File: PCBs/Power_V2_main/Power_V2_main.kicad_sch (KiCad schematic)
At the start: 3 parts

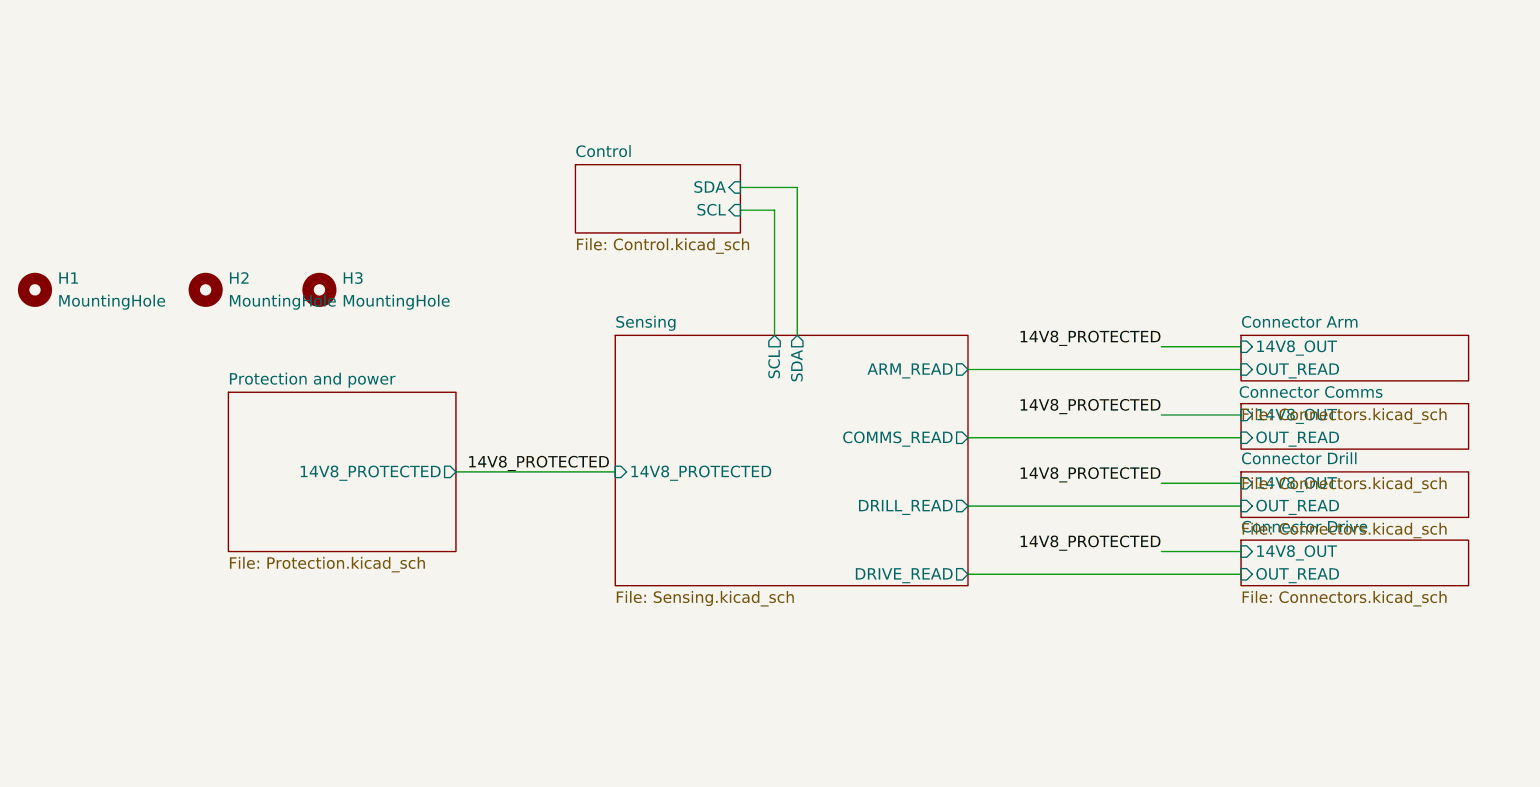
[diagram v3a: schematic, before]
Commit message: added LED indicators to board and redid power distribution in PCIe
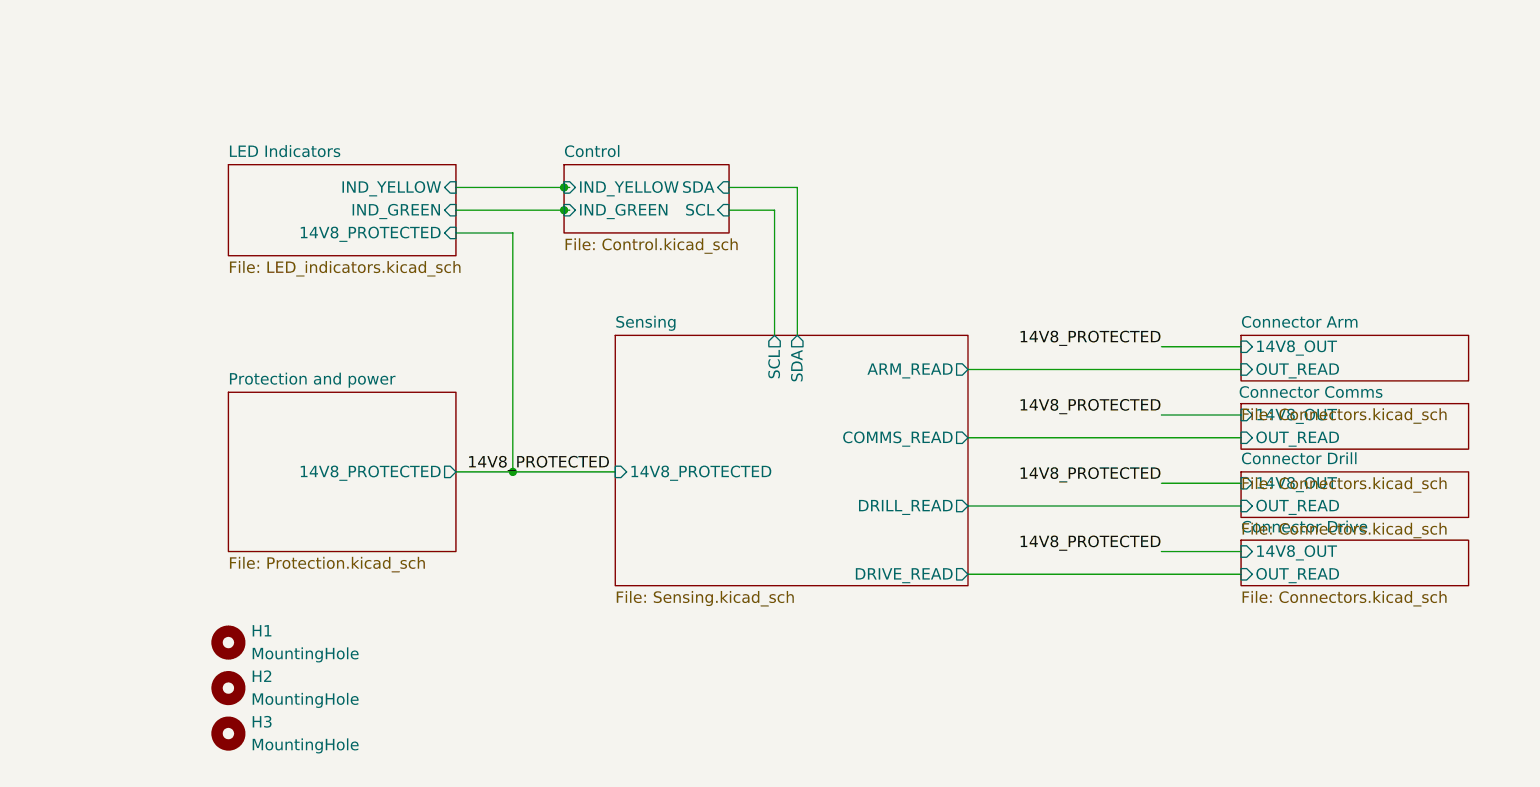
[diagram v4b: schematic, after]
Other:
- added sheet LED Indicators (LED_indicators.kicad_sch)
- sheet Control ports: added IND_GREEN, IND_YELLOW; removed none
- moved on the sheet: H1, H2, H3
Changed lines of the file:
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@@
 	(generator_version "9.0")
 	(paper "A4")
+	(junction
+		(at 120.015 66.04)
+		(diameter 0)
+		(color 0 0 0 0)
+	)
+	(junction
+		(at 120.015 63.5)
+		(diameter 0)
+		(color 0 0 0 0)
+	)
+	(junction
+		(at 114.3 95.25)
+		(diameter 0)
+		(color 0 0 0 0)
+	)
 	(wire
 		(pts
@@
 	(wire
 		(pts
+			(xy 114.3 95.25) (xy 125.73 95.25)
+		)
+		(stroke
+			(width 0)
+			(type default)
+		)
+	)
+	(wire
+		(pts
 			(xy 165.1 91.44) (xy 195.58 91.44)
 		)
@@
 	(wire
 		(pts
+			(xy 120.015 63.5) (xy 120.65 63.5)
+		)
+		(stroke
+			(width 0)
+			(type default)
+		)
+	)
+	(wire
+		(pts
+			(xy 107.95 66.04) (xy 120.015 66.04)
+		)
+		(stroke
+			(width 0)
+			(type default)
+		)
+	)
+	(wire
+		(pts
+			(xy 114.3 68.58) (xy 114.3 95.25)
+		)
+		(stroke
+			(width 0)
+			(type default)
+		)
+	)
+	(wire
+		(pts
 			(xy 165.1 106.68) (xy 195.58 106.68)
 		)
@@
 	(wire
 		(pts
+			(xy 120.015 66.04) (xy 120.65 66.04)
+		)
+		(stroke
+			(width 0)
+			(type default)
+		)
+	)
+	(wire
+		(pts
 			(xy 165.1 83.82) (xy 195.58 83.82)
 		)
@@
 	(wire
 		(pts
-			(xy 139.7 66.04) (xy 143.51 66.04)
+			(xy 107.95 63.5) (xy 120.015 63.5)
+		)
+		(stroke
+			(width 0)
+			(type default)
+		)
+	)
+	(wire
+		(pts
+			(xy 107.95 68.58) (xy 114.3 68.58)
+		)
+		(stroke
+			(width 0)
+			(type default)
+		)
+	)
+	(wire
+		(pts
+			(xy 138.43 66.04) (xy 143.51 66.04)
 		)
 		(stroke
@@
 	(wire
 		(pts
-			(xy 107.95 95.25) (xy 125.73 95.25)
+			(xy 107.95 95.25) (xy 114.3 95.25)
 		)
 		(stroke
@@
 	(wire
 		(pts
-			(xy 139.7 63.5) (xy 146.05 63.5)
+			(xy 138.43 63.5) (xy 146.05 63.5)
 		)
 		(stroke
@@
 	(symbol
 		(lib_id "Mechanical:MountingHole")
-		(at 92.71 74.93 0)
+		(at 82.55 124.46 0)
 		(unit 1)
 		(exclude_from_sim no)
@@
 		(fields_autoplaced yes)
 		(property "Reference" "H3"
-			(at 95.25 73.6599 0)
+			(at 85.09 123.1899 0)
 			(effects
 				(font
@@
 		)
 		(property "Value" "MountingHole"
-			(at 95.25 76.1999 0)
+			(at 85.09 125.7299 0)
 			(effects
 				(font
@@
 		)
 		(property "Footprint" "MountingHole:MountingHole_2.5mm"
-			(at 92.71 74.93 0)
+			(at 82.55 124.46 0)
 			(effects
 				(font
@@
 		)
 		(property "Datasheet" "~"
-			(at 92.71 74.93 0)
+			(at 82.55 124.46 0)
 			(effects
 				(font
@@
 		)
 		(property "Description" "Mounting Hole without connection"
-			(at 92.71 74.93 0)
+			(at 82.55 124.46 0)
 			(effects
 				(font
@@
 	(symbol
 		(lib_id "Mechanical:MountingHole")
-		(at 80.01 74.93 0)
+		(at 82.55 119.38 0)
 		(unit 1)
 		(exclude_from_sim no)
@@
 		(fields_autoplaced yes)
 		(property "Reference" "H2"
-			(at 82.55 73.6599 0)
+			(at 85.09 118.1099 0)
 			(effects
 				(font
@@
 		)
 		(property "Value" "MountingHole"
-			(at 82.55 76.1999 0)
+			(at 85.09 120.6499 0)
 			(effects
 				(font
@@
 		)
 		(property "Footprint" "MountingHole:MountingHole_2.5mm"
-			(at 80.01 74.93 0)
+			(at 82.55 119.38 0)
 			(effects
 				(font
@@
 		)
 		(property "Datasheet" "~"
-			(at 80.01 74.93 0)
+			(at 82.55 119.38 0)
 			(effects
 				(font
@@
 		)
 		(property "Description" "Mounting Hole without connection"
-			(at 80.01 74.93 0)
+			(at 82.55 119.38 0)
 			(effects
 				(font
@@
 	(symbol
 		(lib_id "Mechanical:MountingHole")
-		(at 60.96 74.93 0)
+		(at 82.55 114.3 0)
 		(unit 1)
 		(exclude_from_sim no)
@@
 		(fields_autoplaced yes)
 		(property "Reference" "H1"
-			(at 63.5 73.6599 0)
+			(at 85.09 113.0299 0)
 			(effects
 				(font
@@
 		)
 		(property "Value" "MountingHole"
-			(at 63.5 76.1999 0)
+			(at 85.09 115.5699 0)
 			(effects
 				(font
@@
 		)
 		(property "Footprint" "MountingHole:MountingHole_2.5mm"
-			(at 60.96 74.93 0)
+			(at 82.55 114.3 0)
 			(effects
 				(font
@@
 		)
 		(property "Datasheet" "~"
-			(at 60.96 74.93 0)
+			(at 82.55 114.3 0)
 			(effects
 				(font
@@
 		)
 		(property "Description" "Mounting Hole without connection"
-			(at 60.96 74.93 0)
+			(at 82.55 114.3 0)
 			(effects
 				(font
@@
 	)
 	(sheet
-		(at 121.285 60.96)
+		(at 120.015 60.96)
 		(size 18.415 7.62)
 		(exclude_from_sim no)
@@
 		)
 		(property "Sheetname" "Control"
-			(at 121.285 60.2484 0)
+			(at 120.015 60.2484 0)
 			(effects
 				(font
@@
 		)
 		(property "Sheetfile" "Control.kicad_sch"
-			(at 121.285 69.1646 0)
+			(at 120.015 69.1646 0)
 			(effects
 				(font
@@
 		)
 		(pin "SCL" input
-			(at 139.7 66.04 0)
+			(at 138.43 66.04 0)
 			(effects
 				(font
@@
 		)
 		(pin "SDA" input
-			(at 139.7 63.5 0)
-			(effects
-				(font
-					(size 1.27 1.27)
-				)
-				(justify right)
+			(at 138.43 63.5 0)
+			(effects
+				(font
+					(size 1.27 1.27)
+				)
+				(justify right)
+			)
+		)
+		(pin "IND_GREEN" input
+			(at 120.015 66.04 180)
+			(effects
+				(font
+					(size 1.27 1.27)
+				)
+				(justify left)
+			)
+		)
+		(pin "IND_YELLOW" input
+			(at 120.015 63.5 180)
+			(effects
+				(font
+					(size 1.27 1.27)
+				)
+				(justify left)
 			)
 		)
@@
 				)
 			)
+		)
+	)
+	(sheet
+		(at 82.55 60.96)
+		(size 25.4 10.16)
+		(exclude_from_sim no)
+		(in_bom yes)
+		(on_board yes)
+		(dnp no)
+		(fields_autoplaced yes)
+		(stroke
+			(width 0.1524)
+			(type solid)
+		)
+		(fill
+			(color 0 0 0 0.0000)
+		)
+		(property "Sheetname" "LED Indicators"
+			(at 82.55 60.2484 0)
+			(effects
+				(font
+					(size 1.27 1.27)
+				)
+				(justify left bottom)
+			)
+		)
+		(property "Sheetfile" "LED_indicators.kicad_sch"
+			(at 82.55 71.7046 0)
+			(effects
+				(font
+					(size 1.27 1.27)
+				)
+				(justify left top)
+			)
+		)
+		(pin "14V8_PROTECTED" input
+			(at 107.95 68.58 0)
+			(effects
+				(font
+					(size 1.27 1.27)
+				)
+				(justify right)
+			)
+		)
+		(pin "IND_GREEN" input
+			(at 107.95 66.04 0)
+			(effects
+				(font
+					(size 1.27 1.27)
+				)
+				(justify right)
+			)
+		)
+		(pin "IND_YELLOW" input
+			(at 107.95 63.5 0)
+			(effects
+				(font
+					(size 1.27 1.27)
+				)
+				(justify right)
+			)
+		)
+		(instances
+			(project "Power_V2_main"
+				(path "/68375d53-ee5f-4f08-9b72-814cdcf8200e"
+					(page "9")
+				)
+			)

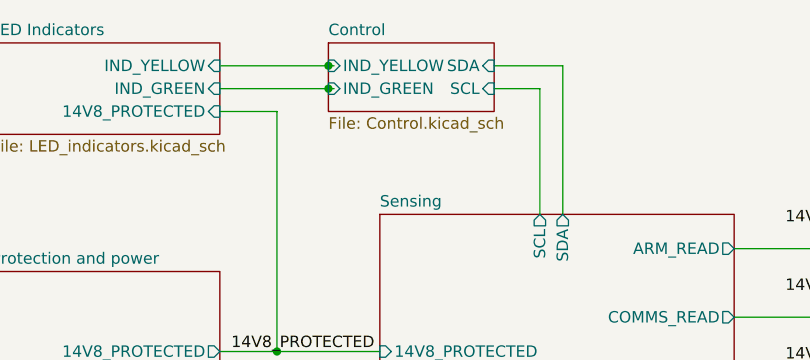
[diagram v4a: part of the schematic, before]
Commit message: modification to LED switches
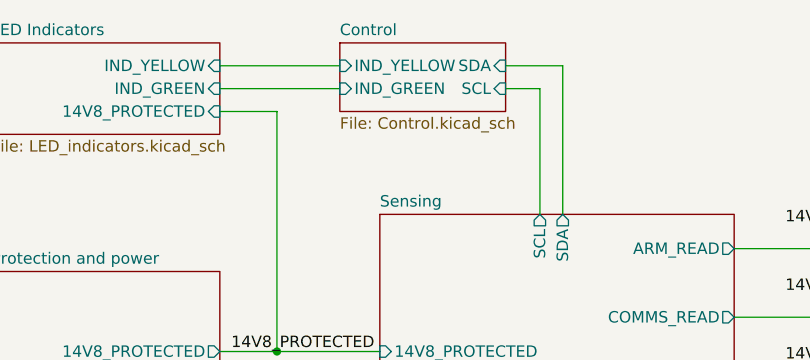
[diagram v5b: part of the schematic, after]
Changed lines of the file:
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@@
 	(paper "A4")
-	(junction
-		(at 120.015 66.04)
-		(diameter 0)
-		(color 0 0 0 0)
-	)
-	(junction
-		(at 120.015 63.5)
-		(diameter 0)
-		(color 0 0 0 0)
-	)
 	(junction
 		(at 114.3 95.25)
@@
 	(wire
 		(pts
-			(xy 120.015 63.5) (xy 120.65 63.5)
-		)
-		(stroke
-			(width 0)
-			(type default)
-		)
-	)
-	(wire
-		(pts
-			(xy 107.95 66.04) (xy 120.015 66.04)
+			(xy 107.95 66.04) (xy 121.285 66.04)
 		)
 		(stroke
@@
 	(wire
 		(pts
-			(xy 120.015 66.04) (xy 120.65 66.04)
-		)
-		(stroke
-			(width 0)
-			(type default)
-		)
-	)
-	(wire
-		(pts
 			(xy 165.1 83.82) (xy 195.58 83.82)
 		)
@@
 	(wire
 		(pts
-			(xy 107.95 63.5) (xy 120.015 63.5)
+			(xy 107.95 63.5) (xy 121.285 63.5)
 		)
 		(stroke
@@
 	(wire
 		(pts
-			(xy 138.43 66.04) (xy 143.51 66.04)
+			(xy 139.7 66.04) (xy 143.51 66.04)
 		)
 		(stroke
@@
 	(wire
 		(pts
-			(xy 138.43 63.5) (xy 146.05 63.5)
+			(xy 139.7 63.5) (xy 146.05 63.5)
 		)
 		(stroke
@@
 	)
 	(sheet
-		(at 120.015 60.96)
+		(at 121.285 60.96)
 		(size 18.415 7.62)
 		(exclude_from_sim no)
@@
 		)
 		(property "Sheetname" "Control"
-			(at 120.015 60.2484 0)
+			(at 121.285 60.2484 0)
 			(effects
 				(font
@@
 		)
 		(property "Sheetfile" "Control.kicad_sch"
-			(at 120.015 69.1646 0)
+			(at 121.285 69.1646 0)
 			(effects
 				(font
@@
 		)
 		(pin "SCL" input
-			(at 138.43 66.04 0)
+			(at 139.7 66.04 0)
 			(effects
 				(font
@@
 		)
 		(pin "SDA" input
-			(at 138.43 63.5 0)
+			(at 139.7 63.5 0)
 			(effects
 				(font
@@
 		)
 		(pin "IND_GREEN" input
-			(at 120.015 66.04 180)
+			(at 121.285 66.04 180)
 			(effects
 				(font
@@
 		)
 		(pin "IND_YELLOW" input
-			(at 120.015 63.5 180)
-			(effects
-				(font
+			(at 121.285 63.5 180)
+			(effects
+				(font

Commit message: follow up changes from meeting
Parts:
- H1, H2, H3: footprint MountingHole:MountingHole_2.5mm -> MountingHole:MountingHole_2.7mm_M2.5_DIN965_Pad_TopBottom
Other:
- sheet Control ports: added IND_SIREN; removed none
- sheet LED Indicators ports: added IND_SIREN; removed none
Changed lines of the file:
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@@
 	(wire
 		(pts
-			(xy 114.3 68.58) (xy 114.3 95.25)
+			(xy 114.3 71.12) (xy 114.3 95.25)
 		)
 		(stroke
@@
 	(wire
 		(pts
+			(xy 107.95 68.58) (xy 121.285 68.58)
+		)
+		(stroke
+			(width 0)
+			(type default)
+		)
+	)
+	(wire
+		(pts
 			(xy 107.95 63.5) (xy 121.285 63.5)
 		)
@@
 	(wire
 		(pts
-			(xy 107.95 68.58) (xy 114.3 68.58)
+			(xy 107.95 71.12) (xy 114.3 71.12)
 		)
 		(stroke
@@
 			)
 		)
-		(property "Footprint" "MountingHole:MountingHole_2.5mm"
+		(property "Footprint" "MountingHole:MountingHole_2.7mm_M2.5_DIN965_Pad_TopBottom"
 			(at 82.55 124.46 0)
 			(effects
@@
 			)
 		)
-		(property "Footprint" "MountingHole:MountingHole_2.5mm"
+		(property "Footprint" "MountingHole:MountingHole_2.7mm_M2.5_DIN965_Pad_TopBottom"
 			(at 82.55 119.38 0)
 			(effects
@@
 			)
 		)
-		(property "Footprint" "MountingHole:MountingHole_2.5mm"
+		(property "Footprint" "MountingHole:MountingHole_2.7mm_M2.5_DIN965_Pad_TopBottom"
 			(at 82.55 114.3 0)
 			(effects
@@
 	(sheet
 		(at 121.285 60.96)
-		(size 18.415 7.62)
+		(size 18.415 10.16)
 		(exclude_from_sim no)
 		(in_bom yes)
@@
 		)
 		(property "Sheetfile" "Control.kicad_sch"
-			(at 121.285 69.1646 0)
+			(at 121.285 71.7046 0)
 			(effects
 				(font
@@
 		(pin "IND_YELLOW" input
 			(at 121.285 63.5 180)
+			(effects
+				(font
+					(size 1.27 1.27)
+				)
+				(justify left)
+			)
+		)
+		(pin "IND_SIREN" input
+			(at 121.285 68.58 180)
 			(effects
 				(font
@@
 	(sheet
 		(at 82.55 60.96)
-		(size 25.4 10.16)
+		(size 25.4 11.43)
 		(exclude_from_sim no)
 		(in_bom yes)
@@
 		)
 		(property "Sheetfile" "LED_indicators.kicad_sch"
-			(at 82.55 71.7046 0)
+			(at 82.55 72.9746 0)
 			(effects
 				(font
@@
 		)
 		(pin "14V8_PROTECTED" input
-			(at 107.95 68.58 0)
+			(at 107.95 71.12 0)
 			(effects
 				(font
@@
 			(effects
 				(font
+					(size 1.27 1.27)
+				)
+				(justify right)
+			)
+		)
+		(pin "IND_SIREN" input
+			(at 107.95 68.58 0)
+			(effects
+				(font
